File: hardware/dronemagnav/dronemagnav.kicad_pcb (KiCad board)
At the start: 4 copper layers, 64 x 60 mm, 60 parts, among them J1 USB-C, J2 FC_TELEM, J3 microSD, J4 GNSS_ANT, J5 SENSOR_MAST, SW1 RESET, SW2 BOOT, U1 ESP32-S3-WROOM-1-N16R8, U2 BMI088, U3 LIS3MDL, U4 BMP280, U5 MAX-M10S, U6 AMS1117-3.3, U7 AP2112K-3.3, U8 USBLC6-2SC6

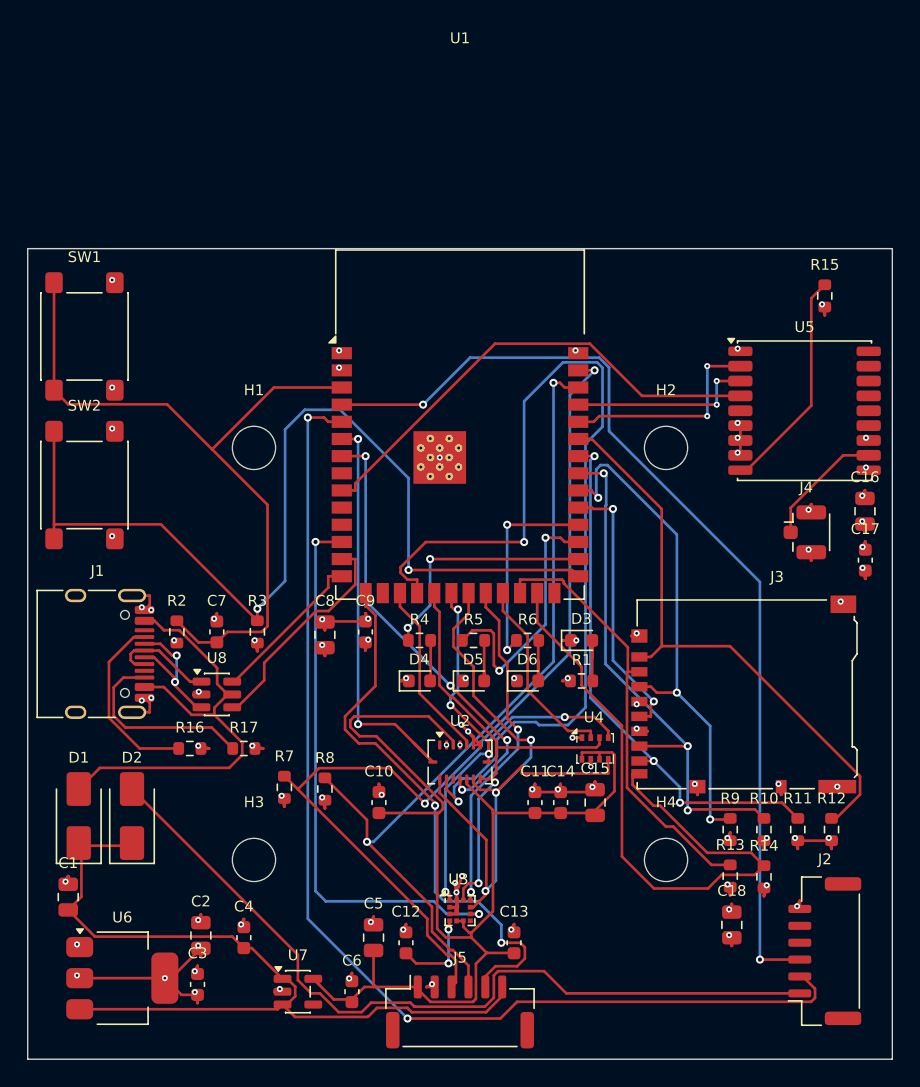
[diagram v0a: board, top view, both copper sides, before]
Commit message: Move power vias out of pads, add fabrication notes, close the MAX-M10S strap question
Auditing the routed board showed the power fanout had put 77 GND/+3V3 vias
inside their own pads (not just the two BMI088 pads the docs mentioned):
its candidate search started 0.25 mm from the pad centre and only checked
other-net copper.

- tools/dogbone_vias.py: two-pass (remove / add) re-fanout. 74 vias now sit
  outside their pads on short stubs; pads matched by position (SW/J3/J4 have
  duplicate pad numbers), keep-outs tested with the real polygons, stubs
  checked too, board-edge margin honoured. Three vias have provably no room
  (BMI088 pads 2/4 between 0.5 mm-pitch escapes over the body keep-out, and
  the microSD VDD pad fenced by SD_D3) and stay in pad at 0.4 mm; two remain
  in thermal pads. DRC: 0 unconnected, 0 electrical (22 silk cosmetics).
- tools/fab_audit.py + tools/make_fab.py: regenerate Gerbers, drill, pick and
  place, renders, and a FABRICATION-NOTES.md (stackup, limits, the exact
  via-in-pad list with a fill-and-cap requirement, assembly notes), packed
  into the Gerber ZIP.
- MAX-M10S: checked against the u-blox integration manual UBX-20053088 R05.
  VIO_SEL open selects 3.3 V I/O, which is what the board supplies, so the
  schematic is correct as built. TIMEPULSE is tied to SAFEBOOT_N inside the
  module, so the firmware now configures GPIO16 input-only with a comment.
- README, design spec and design PDF updated accordingly.

Co-Authored-By: Claude Fable 5.1 <noreply@anthropic.com>
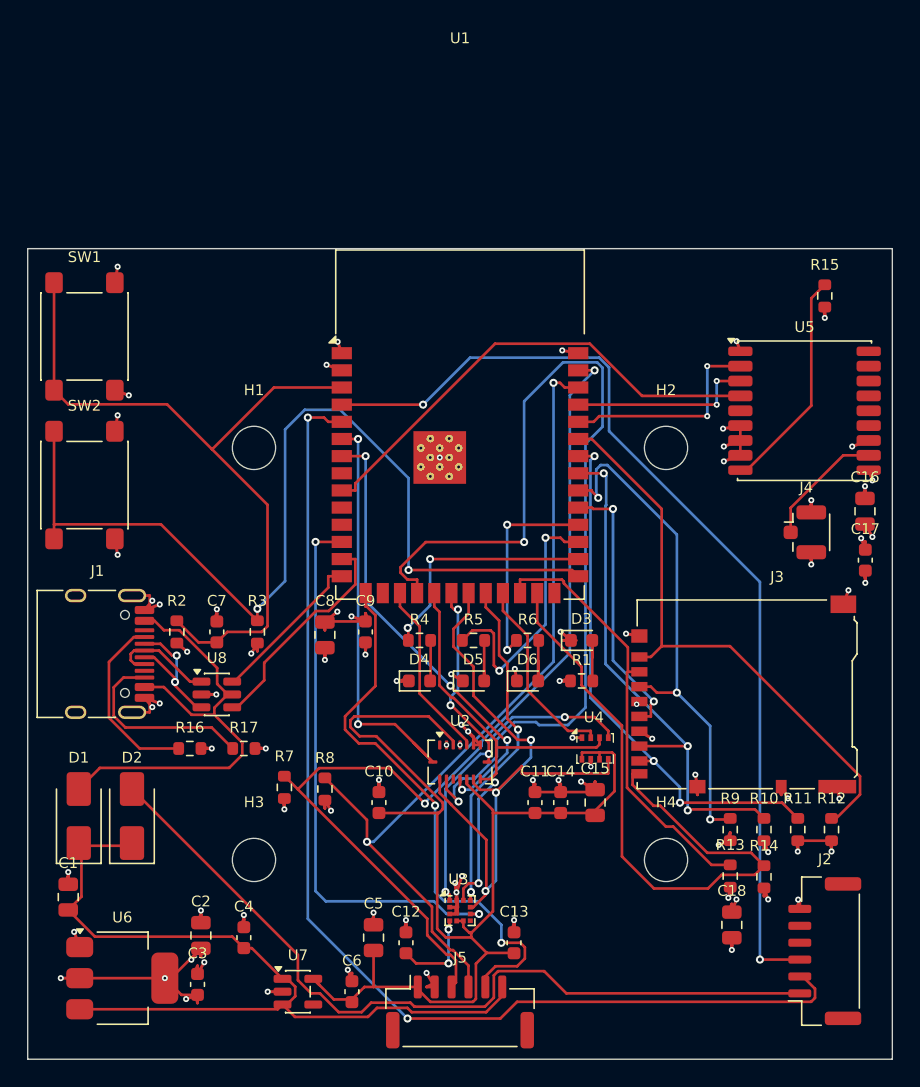
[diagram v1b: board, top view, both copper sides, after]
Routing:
- net GND: track 82.4 -> 108.5 mm
- net +3V3: track 48.2 -> 65.9 mm
